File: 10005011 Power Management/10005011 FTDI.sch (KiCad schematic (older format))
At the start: 49 parts, among them IC11 TPS5430DDA, IC12 LM4120AIM5-3.0, IC26 NC7SZ66, IC27 NC7SZ66, IC4 FT2232, IC8 LF33CDT, J1 USB Mini B, Q1 6 MHz

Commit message: Powermanagement dev
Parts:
- C1, C124, C3, C5: value 0.1uF -> 100nF; symbol 10005011_Power_Management_Schematic_Symbols:0.1uF -> Device:C; Bom_Footprint 0402 -> (none); Description CAP CER 47PF 50V C0G/NP0 0402 -> CAPACITOR,100NF,16V,+/-10%,X7R,0402; Item Number (none) -> 10022607; Manufacturer (none) -> MURATA; Manufacturer_No (none) -> GRM155R71C104JA88J
- C126, C35, C36, C46, C58, C59: Description (none) -> CAPACITOR,100NF,16V,+/-10%,X7R,0402; Item Number (none) -> 10022607; Manufacturer (none) -> MURATA; Manufacturer_No (none) -> GRM155R71C104JA88J
- C127, C128: symbol 10005011_Power_Management_Schematic_Symbols:47pF -> Device:C
- C2: symbol 10005011_Power_Management_Schematic_Symbols:0.01uF -> Device:C
- C44, C54: symbol Device:CP -> 10005011_Power_Management:CP
- C55: Description (none) -> CAPACITOR CERAMIC, 100NF, +/-10%, 50V, X7R,0805; Item Number (none) -> 10022135
- D11: symbol 10005011_Power_Management_Schematic_Symbols:STPS340U -> 10005011_Power_Management:STPS340U; Description DIODE SCHOTTKY 40V 3A SMB -> DIODE SCHOTTKY, 3A, 40V; Item Number (none) -> 10022656; Manufacturer (none) -> STMICROELECTRONICS; Manufacturer_No (none) -> STPS340U; Mfgr STMicroelectronics -> (none); Mfgr_PN STPS340U -> (none)
- D16: symbol 10005011_Power_Management_Schematic_Symbols:BAT54C -> 10005011_Power_Management:BAT54C; BOM_Footprint SOT23 -> (none); Item Number (none) -> 10022653
- IC12: symbol page3:LM4120AIM5-3.0 -> 10005011_Power_Management:LM4120AIM5-3.0; Description (none) -> IC,VOLTAGE REFERENCE,5MA,3V +/-2%,SOT23; Item Number (none) -> 10022896; MNF TI -> (none); MNF PN LM4120AIM5-3.0 -> (none); Manufacturer (none) -> NATIONAL SEMICONDUCTOR; Manufacturer_No (none) -> LM4120AIM5-3.0/NOPB
- IC26, IC27: symbol page3:NC7SZ66 -> 10005011_Power_Management:NC7SZ66; Description (none) -> IC,BUS SWITCH,SC70; Item Number (none) -> 10039588; Manufacturer (none) -> FAIRCHILD SEMICONDUCTOR; Manufacturer_No (none) -> NC7SZ66P5X
- J1: symbol page3:USB_B_Mini_2shield -> 10005011_Power_Management:USB_B_Mini_2shield; Description (none) -> USB MINI B; Item Number (none) -> 10022867; Manufacturer (none) -> MOLEX; Manufacturer_No (none) -> 54819-0519
- L1: symbol 10005011_Power_Management_Schematic_Symbols:MH2029-221Y -> Device:Ferrite_Bead_Small
- L7: symbol 10005011_Power_Management_Schematic_Symbols:MH2029-221Y -> Device:Ferrite_Bead_Small; Bom_Footprint 0805 -> (none); Item Number (none) -> 10039587
- L8: symbol page3:Common_Mode_Choke -> 10005011_Power_Management:DLP31SN551ML2L; Description (none) -> COMMON MODE CHOKE COIL 550OHM; Item Number (none) -> 10039588; Manufacturer (none) -> MURATA; Manufacturer_No (none) -> DLP31SN551ML2L
- ML1: symbol 10005011_Power_Management_Schematic_Symbols:B72500T0040M060 -> Device:Varistor; Bom_Footprint 0603 -> (none); Description VARISTOR 8V 30A 0603 -> SMD VARISTOR, 5.5V,C0603; Item Number (none) -> 10022926
- PG1: renamed from PG2; symbol 10005011_Power_Management_Schematic_Symbols:82356050050 -> Device:D_TVS; Description ESD SUPPRESSOR 0603; 5VDC; 5PF -> VARISTOR, CMS PROTECTION ESD SURGE SUPPRESSOR,C0603; Item Number (none) -> 10022946
- PG2: renamed from PG1; symbol 10005011_Power_Management_Schematic_Symbols:82356050050 -> Device:D_TVS; Description ESD SUPPRESSOR 0603; 5VDC; 5PF -> VARISTOR, CMS PROTECTION ESD SURGE SUPPRESSOR,C0603; Item Number (none) -> 10022946
- R56, R57: value 10k_0.1pcnt -> 10k; symbol 10005011_Power_Management_Schematic_Symbols:10k_0.1pcnt -> Device:R
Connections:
- net labels added: 0VANA
- net labels removed: GNDA
- wire segments 235 -> 237
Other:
- moved on the sheet: C126, C34, C35, C36, C45, C46, C47, C55, C57, C58, C59, C7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

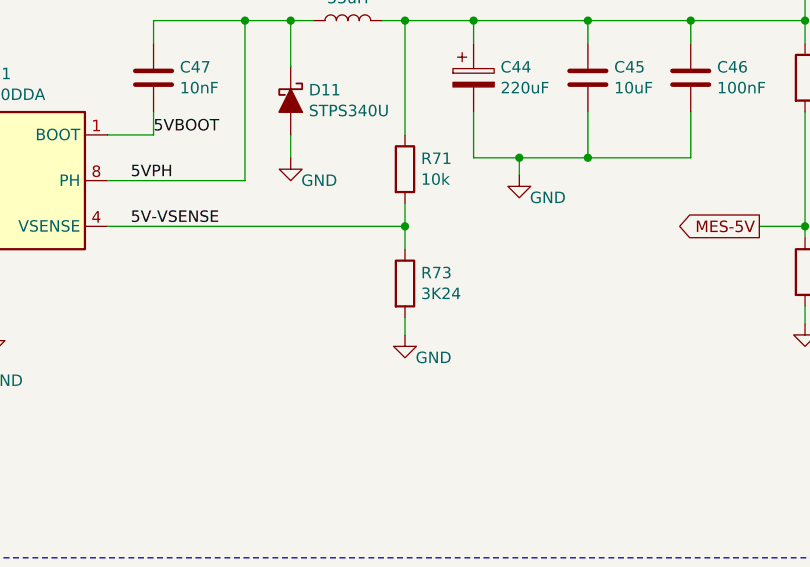
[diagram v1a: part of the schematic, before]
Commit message: update PCB deleting double lines in the edge layer to create a board outline and update the USB_A footprints and IC11
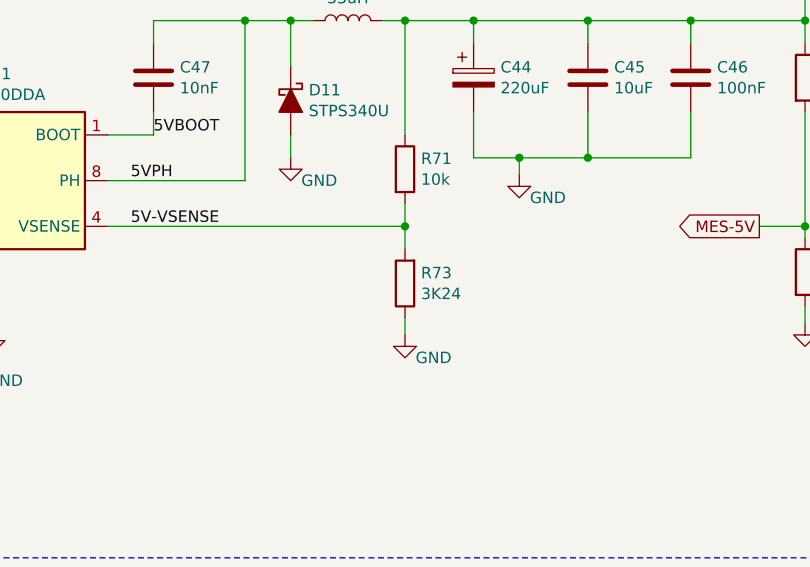
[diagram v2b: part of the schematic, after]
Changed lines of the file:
@@
 U 1 1 5FDD612C
 P 13900 5450
-F 0 "R73" H 13970 5496 50  0000 L CNN
-F 1 "3K24" H 13970 5405 50  0000 L CNN
+F 0 "R73" H 13830 5404 50  0000 R CNN
+F 1 "3K24" H 13830 5495 50  0000 R CNN
 F 2 "10005011 Power Management:R0603_1" V 13830 5450 50  0001 C CNN
 F 3 "https://www.yageo.com/upload/media/product/productsearch/datasheet/rchip/PYu-RT_1-to-0.01_RoHS_L_11.pdf" H 13900 5450 50  0001 C CNN
@@
 F 5 "RT0603BRD073K24L" H 13900 5450 50  0001 C CNN "Mnf PN"
 	1    13900 5450
-	1    0    0    -1
+	-1   0    0    1
 $EndComp
 $Comp
@@
 U 1 1 5E978E52
 P 14700 4550
-F 0 "C45" H 14815 4596 50  0000 L CNN
-F 1 "10uF" H 14815 4505 50  0000 L CNN
+F 0 "C45" H 14815 4504 50  0000 L CNN
+F 1 "10uF" H 14815 4595 50  0000 L CNN
 F 2 "10005011 Power Management:C0805-AIROX-KEMET-C0805C106KA3" H 14738 4400 50  0001 C CNN
 F 3 "https://api.kemet.com/component-edge/download/datasheet/C0805C106K4PACTU.pdf" H 14700 4550 50  0001 C CNN
@@
 F 5 "C0805C106K4PAC" H 14700 4550 50  0001 C CNN "Mnf PN"
 	1    14700 4550
-	1    0    0    -1
+	1    0    0    1
 $EndComp
 $Comp
@@
 U 1 1 5FDD6122
 P 15150 4550
-F 0 "C46" H 15265 4596 50  0000 L CNN
-F 1 "100nF" H 15265 4505 50  0000 L CNN
+F 0 "C46" H 15265 4504 50  0000 L CNN
+F 1 "100nF" H 15265 4595 50  0000 L CNN
 F 2 "10005011 Power Management:C0402_1" H 15188 4400 50  0001 C CNN
 F 3 "~" H 15150 4550 50  0001 C CNN
@@
 F 9 "GRM155R71C104JA88J" H 15150 4550 50  0001 C CNN "Manufacturer_No"
 	1    15150 4550
-	1    0    0    -1
+	1    0    0    1
 $EndComp
 $Comp
@@
 U 1 1 5EE61C58
 P 12800 4550
-F 0 "C47" H 12685 4504 50  0000 R CNN
-F 1 "10nF" H 12685 4595 50  0000 R CNN
+F 0 "C47" H 12685 4596 50  0000 R CNN
+F 1 "10nF" H 12685 4505 50  0000 R CNN
 F 2 "10005011 Power Management:C0603_1" H 12838 4400 50  0001 C CNN
 F 3 "http://datasheet.octopart.com/223858615636-Yageo-datasheet-500777.pdf" H 12800 4550 50  0001 C CNN
@@
 F 5 "" H 12800 4550 50  0001 C CNN "Mnf PN"
 	1    12800 4550
-	-1   0    0    1
-$EndComp
-Wire Wire Line
+	-1   0    0    -1
+$EndComp
+Wire Wire Line

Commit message: change CR1-BIS to ZCR1 so that kicad does not think it is missing annotation, do the same in the PCB to be able to read netlist without components getting erased and placed new
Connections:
- wire segments 237 -> 238
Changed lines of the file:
@@
 P 4400 4550
 F 0 "Q1" V 4350 4200 50  0000 L CNN
-F 1 "6 MHz" V 4450 4150 50  0000 L CNN
+F 1 "6 MHz" V 4450 4050 50  0000 L CNN
 F 2 "10005011 Power Management:CSTCR_1" H 4400 4550 50  0001 C CNN
 F 3 "https://www.murata.com/products/productdata/8801051869214/SPEC-CSTCR6M00G53-R0.pdf" H 4400 4550 50  0001 C CNN
 	1    4400 4550
-	0    1    1    0
+	0    1    -1   0
 $EndComp
 $Comp
@@
 	1    0    0    -1
 $EndComp
-Text GLabel 14400 8150 2    50   Output ~ 0
-+3.0VREF
 Text GLabel 11500 5200 0    50   Input ~ 0
 START-5V
@@
 $EndComp
 $Comp
-L power:+3.3V #PWR0203
+L 10005011_Power_Management:+3.3V #PWR0203
 U 1 1 5F11788F
 P 12800 1750
@@
 	5600 1700 4400 1700
 Connection ~ 4400 1700
+$Comp
+L 10005011_Power_Management:+3.0VREF #PWR0287
+U 1 1 5EA5BF85
+P 14400 8100
+F 0 "#PWR0287" H 14400 7950 50  0001 C CNN
+F 1 "+3.0VREF" H 14415 8273 50  0000 C CNN
+F 2 "" H 14400 8100 50  0001 C CNN
+F 3 "" H 14400 8100 50  0001 C CNN
+	1    14400 8100
+	1    0    0    -1
+$EndComp
+Wire Wire Line
+	14400 8100 14400 8150
 $EndSCHEMATC

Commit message: Powermanagement dev, ERC
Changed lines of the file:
@@
 $EndComp
 Wire Wire Line
-	13900 4300 14200 4300
+	13900 4300 14050 4300
 Wire Wire Line
 	15150 4300 15150 4400
@@
 	5800 2050 5800 2150
 Wire Wire Line
-	5600 2150 5600 1700
-Wire Wire Line
 	5600 1700 4400 1700
 Connection ~ 4400 1700
@@
 Wire Wire Line
 	14400 8100 14400 8150
+$Comp
+L power:PWR_FLAG #FLG?
+U 1 1 5EED3856
+P 5800 1450
+AR Path="/5FEC5422/5EED3856" Ref="#FLG?"  Part="1"
+AR Path="/5FDBA600/5EED3856" Ref="#FLG0110"  Part="1"
+F 0 "#FLG0110" H 5800 1525 50  0001 C CNN
+F 1 "PWR_FLAG" H 5800 1600 50  0000 C CNN
+F 2 "" H 5800 1450 50  0001 C CNN
+F 3 "~" H 5800 1450 50  0001 C CNN
+	1    5800 1450
+	1    0    0    -1
+$EndComp
+Wire Wire Line
+	5800 1450 5800 1600
+Connection ~ 5800 1600
+Connection ~ 8750 2150
+$Comp
+L power:PWR_FLAG #FLG?
+U 1 1 5EEE3CA6
+P 8750 2000
+AR Path="/5FEC5422/5EEE3CA6" Ref="#FLG?"  Part="1"
+AR Path="/5FDBA600/5EEE3CA6" Ref="#FLG0111"  Part="1"
+F 0 "#FLG0111" H 8750 2075 50  0001 C CNN
+F 1 "PWR_FLAG" H 8750 2150 50  0000 C CNN
+F 2 "" H 8750 2000 50  0001 C CNN
+F 3 "~" H 8750 2000 50  0001 C CNN
+	1    8750 2000
+	1    0    0    -1
+$EndComp
+Wire Wire Line
+	8750 2000 8750 2150
+$Comp
+L power:PWR_FLAG #FLG?
+U 1 1 5EEFAEE2
+P 14050 4150
+AR Path="/5FEC5422/5EEFAEE2" Ref="#FLG?"  Part="1"
+AR Path="/5FDBA600/5EEFAEE2" Ref="#FLG0112"  Part="1"
+F 0 "#FLG0112" H 14050 4225 50  0001 C CNN
+F 1 "PWR_FLAG" H 14050 4300 50  0000 C CNN
+F 2 "" H 14050 4150 50  0001 C CNN
+F 3 "~" H 14050 4150 50  0001 C CNN
+	1    14050 4150
+	1    0    0    -1
+$EndComp
+Wire Wire Line
+	14050 4150 14050 4300
+Connection ~ 14050 4300
+Wire Wire Line
+	14050 4300 14200 4300
+$Comp
+L power:PWR_FLAG #FLG?
+U 1 1 5F345046
+P 5300 1950
+AR Path="/5FEC5422/5F345046" Ref="#FLG?"  Part="1"
+AR Path="/5FDBA600/5F345046" Ref="#FLG0126"  Part="1"
+F 0 "#FLG0126" H 5300 2025 50  0001 C CNN
+F 1 "PWR_FLAG" H 5300 2100 50  0000 C CNN
+F 2 "" H 5300 1950 50  0001 C CNN
+F 3 "~" H 5300 1950 50  0001 C CNN
+	1    5300 1950
+	1    0    0    -1
+$EndComp
+Wire Wire Line
+	5300 1950 5300 2050
+Wire Wire Line
+	5300 2050 5600 2050
+Connection ~ 5600 2050
+Wire Wire Line
+	5600 2050 5600 1700
+Wire Wire Line
+	5600 2050 5600 2150
 $EndSCHEMATC

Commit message: rename DPAK
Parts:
- IC8: footprint 10005011 Power Management:DPAK_1 -> 10005011 Power Management:DPAK_1b

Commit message: update fp path
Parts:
- C1, C124, C126, C127, C128, C3, C35, C36, C46, C5, C58, C59: footprint 10005011 Power Management:C0402_1 -> AllModules:C0402_1
- C2, C45: footprint 10005011 Power Management:C0805-AIROX-KEMET-C0805C106KA3 -> AllModules:C0805-AIROX-KEMET-C0805C106KA3
- C34: footprint 10005011 Power Management:C1210_1 -> AllModules:C1210_1
- C44, C54: footprint 10005011 Power Management:C-SC8_1 -> AllModules:C-SC8_1
- C47, C7: footprint 10005011 Power Management:C0603_1 -> AllModules:C0603_1
- C55, C57: footprint 10005011 Power Management:C0805_1 -> AllModules:C0805_1
- D11: footprint 10005011 Power Management:SMB_1 -> AllModules:SMB_1
- D16: footprint 10005011 Power Management:SOT23-1G_1 -> AllModules:SOT23-1G_1
- IC11: footprint 10005011 Power Management:SO08-PPAD_COMPOSANT_1 -> AllModules:SO08-PPAD_COMPOSANT_1
- IC12: footprint 10005011 Power Management:SOT23-5_1 -> AllModules:SOT23-5_1
- IC26, IC27: footprint 10005011 Power Management:SC70-5_1 -> AllModules:SC70-5_1
- IC4: footprint 10005011 Power Management:LQFP48-PAD0.28X1.2_1 -> AllModules:LQFP48-PAD0.28X1.2_1
- IC8: footprint 10005011 Power Management:DPAK_1b -> AllModules:DPAK_1b
- J1: footprint 10005011 Power Management:MOL54819-0511_1 -> AllModules:MOL54819-0511_1
- L1, L7: footprint 10005011 Power Management:C0805-AIROX-MURATA-BLM21PG221D -> AllModules:C0805-AIROX-MURATA-BLM21PG221D
- L2: footprint 10005011 Power Management:WE-PD4_1 -> AllModules:WE-PD4_1
- L8: footprint 10005011 Power Management:DLP31S-AIROX_1 -> AllModules:DLP31S-AIROX_1
- ML1, PG1, PG2, R113, R5, R56, R57, R6, R7, R70, R71, R72, R73: footprint 10005011 Power Management:R0603_1 -> AllModules:R0603_1
- Q1: footprint 10005011 Power Management:CSTCR_1 -> AllModules:CSTCR_1
- R3: footprint 10005011 Power Management:R0805_1 -> AllModules:R0805_1
